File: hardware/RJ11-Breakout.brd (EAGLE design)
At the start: 21.6 x 20.3 mm, 8 parts

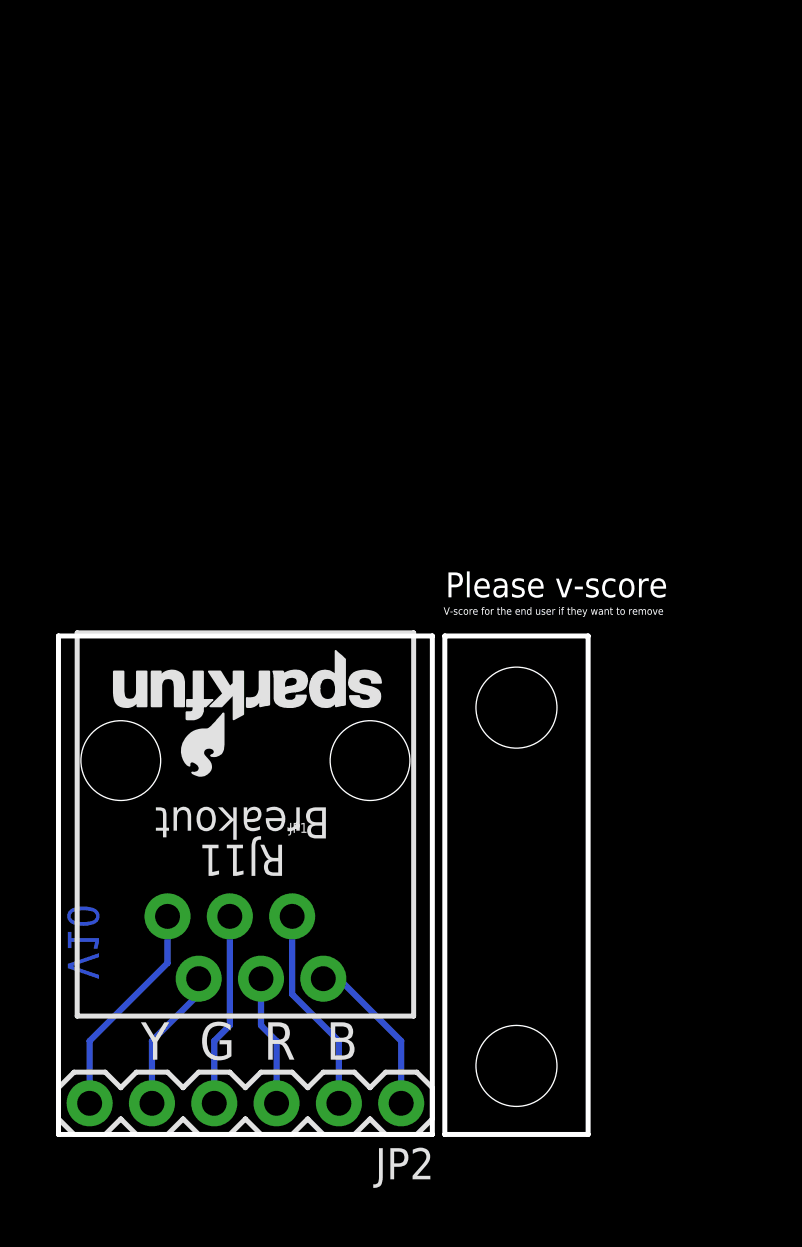
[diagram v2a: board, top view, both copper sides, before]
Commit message: Creating panel of two
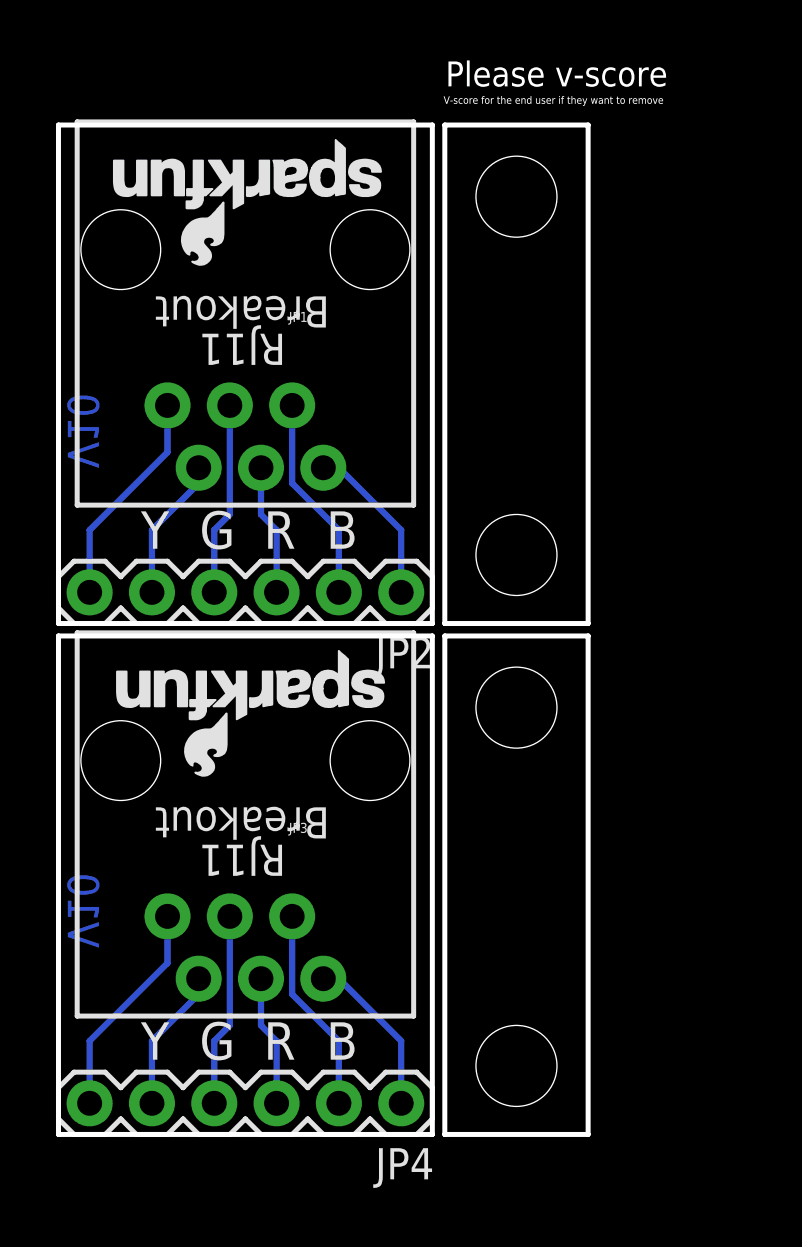
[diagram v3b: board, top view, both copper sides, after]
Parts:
- added H2, H4: STAND-OFF, SparkFun-Electromechanical:STAND-OFF
- added JP3: RJ11, SparkFun-Connectors:RJ11-6
- added JP4: Pins, SparkFun-Connectors:1X06
- added LOGO4, LOGO5: SFE_LOGO_NAME_FLAME.1_INCH, SparkFun-Aesthetics:SFE_LOGO_NAME_FLAME_.1
- added LOGO6: OSHW-LOGOMINI, SparkFun-Aesthetics:OSHW-LOGO-MINI
- moved H1 20.8 mm to (18.7, 23.6)
- moved JP2 20.8 mm to (14.0, 22.1)
- moved LOGO1 20.8 mm to (1.78, 40.6)
- moved LOGO2 20.8 mm to (13.6, 40.6)
- moved LOGO3 20.8 mm to (12.7, 29.7)
- moved H3 20.8 mm to (18.7, 38.2)
- moved JP1 20.8 mm to (7.62, 36.1)
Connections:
- new net BLACK-2: JP1.2, JP2.2
- new net BLUE-2: JP1.6, JP2.6
- new net GREEN-2: JP1.4, JP2.4
- new net RED-2: JP1.3, JP2.3
- new net WHITE-2: JP1.1, JP2.1
- new net YELLOW-2: JP1.5, JP2.5
- net BLACK: now also JP3.2, JP4.2; no longer JP1.2, JP2.2
- net BLUE: now also JP3.6, JP4.6; no longer JP1.6, JP2.6
- net GREEN: now also JP3.4, JP4.4; no longer JP1.4, JP2.4
- net RED: now also JP3.3, JP4.3; no longer JP1.3, JP2.3
- net WHITE: now also JP3.1, JP4.1; no longer JP1.1, JP2.1
- net YELLOW: now also JP3.5, JP4.5; no longer JP1.5, JP2.5
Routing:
- net BLUE-2: track 0.00 -> 8.94 mm
- net BLACK-2: track 0.00 -> 8.41 mm
- net GREEN-2: track 0.00 -> 7.88 mm
- net WHITE-2: track 0.00 -> 6.77 mm
- net YELLOW-2: track 0.00 -> 5.87 mm
- net RED-2: track 0.00 -> 5.34 mm
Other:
- board size 21.6 x 20.3 mm -> 21.6 x 41.1 mm
